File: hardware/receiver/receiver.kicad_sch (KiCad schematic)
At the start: 3 parts, among them J1 Conn_01x07_Socket, J2 Conn_01x02_Socket, U1 Pico

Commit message: Update receiver PCB
Power and ground planes added
Logo and title added to silkscreen
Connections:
- net GND: now also U1.3 (GND), U1.38 (GND)
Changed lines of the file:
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@@
+		)
+	)
+	(label "GND"
+		(at 121.92 78.74 180)
+		(fields_autoplaced yes)
+		(effects
+			(font
+				(size 1.27 1.27)
+			)
+			(justify right bottom)
 		)
 	)
@@
 		)
 	)
+	(label "GND"
+		(at 157.48 78.74 0)
+		(fields_autoplaced yes)
+		(effects
+			(font
+				(size 1.27 1.27)
+			)
+			(justify left bottom)
+		)
+	)

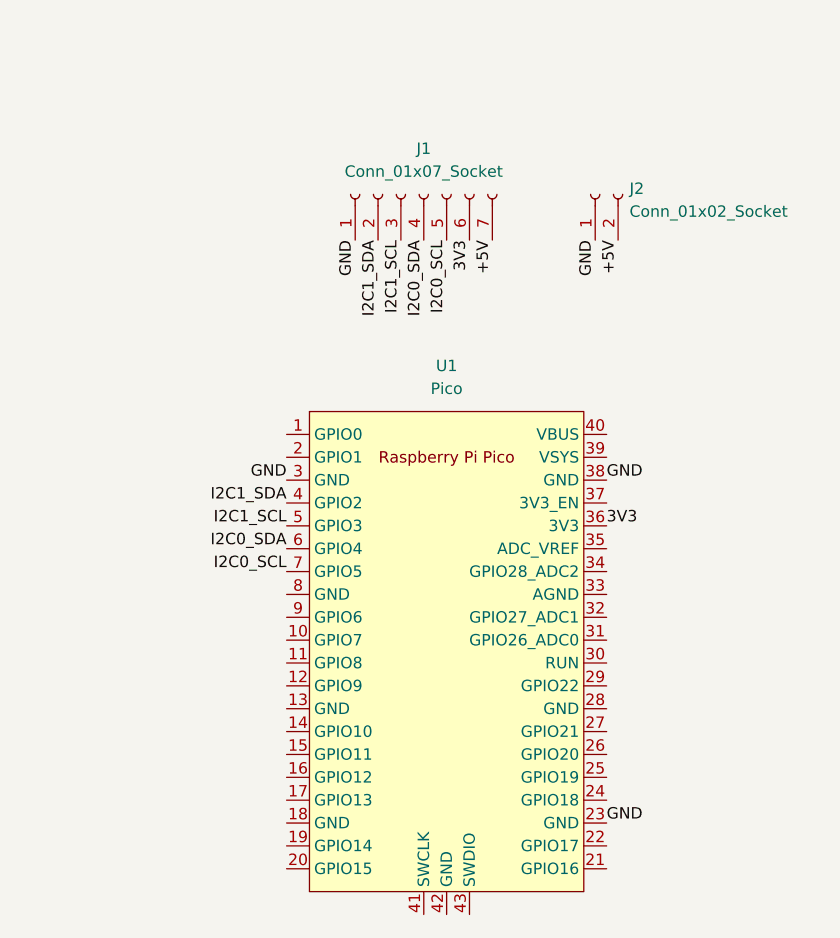
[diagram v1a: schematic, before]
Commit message: Update receiver PCB and add gerber files
Added mounting holes, changes silk screen, and organized the schematic
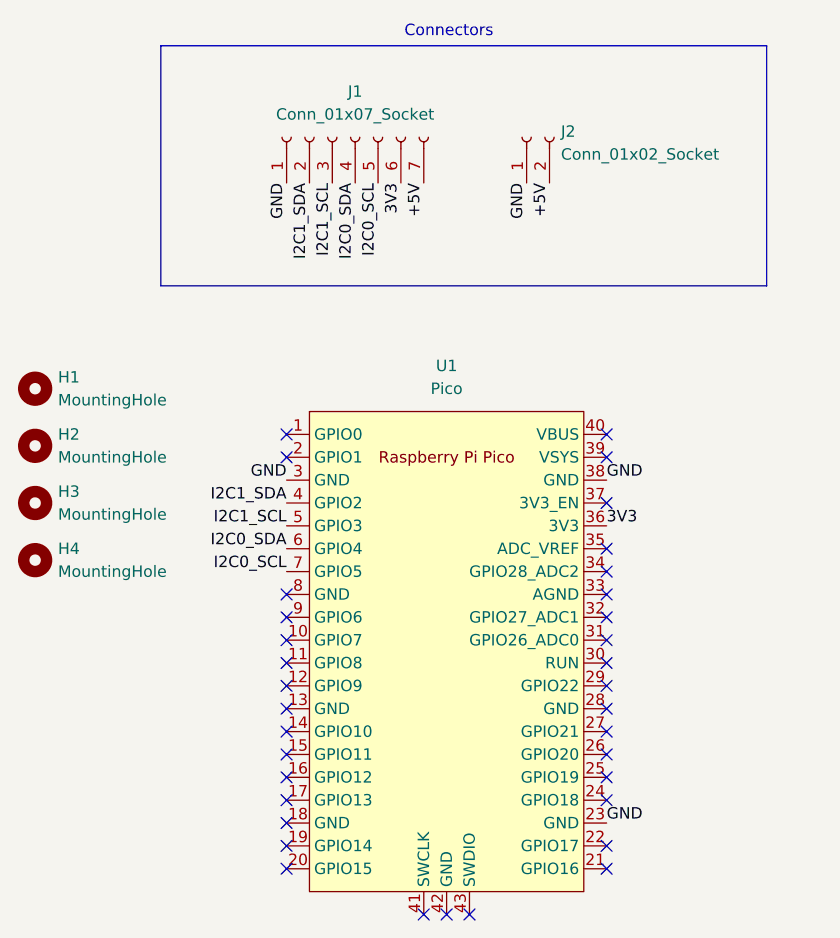
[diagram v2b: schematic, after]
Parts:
- added H1, H2, H3, H4: MountingHole, MountingHole:MountingHole_2.2mm_M2, symbol Mechanical:MountingHole
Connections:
- no-connect marks 0 -> 35
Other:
- note added: "Connectors"
- moved on the sheet: J1, J2
